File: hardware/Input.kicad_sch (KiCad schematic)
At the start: 15 parts, among them J10 Conn_Coaxial, J11 Conn_Coaxial, J12 Conn_Coaxial, J13 Conn_Coaxial, U22 SN74LVC2T45DCTR, U23 SN74LVC2T45DCTR

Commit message: update footprints to meet min pad clearance of 0.2mm
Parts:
- U22, U23: footprint Package_SO:VSSOP-8_2.3x2mm_P0.5mm -> kicad-lib:VSSOP-8_2.3x2mm_P0.5mm_TexasInstruments
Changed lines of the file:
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@@
 			)
 		)
-		(property "Footprint" "Package_SO:VSSOP-8_2.3x2mm_P0.5mm"
+		(property "Footprint" "kicad-lib:VSSOP-8_2.3x2mm_P0.5mm_TexasInstruments"
 			(at 152.4 93.98 0)
 			(effects
@@
 			)
 		)
-		(property "Footprint" "Package_SO:VSSOP-8_2.3x2mm_P0.5mm"
+		(property "Footprint" "kicad-lib:VSSOP-8_2.3x2mm_P0.5mm_TexasInstruments"
 			(at 152.4 152.4 0)
 			(effects

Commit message: update incorrect part numbers to match correct footprints
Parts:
- U22, U23: Link https://www.digikey.com/en/products/detail/texas-instruments/SN74LVC2T45DCTR/639457 -> https://www.digikey.com/en/products/detail/texas-instruments/SN74LVC2T45DCUR/657833; Manufacturer Number SN74LVC2T45DCTR -> SN74LVC2T45DCUR

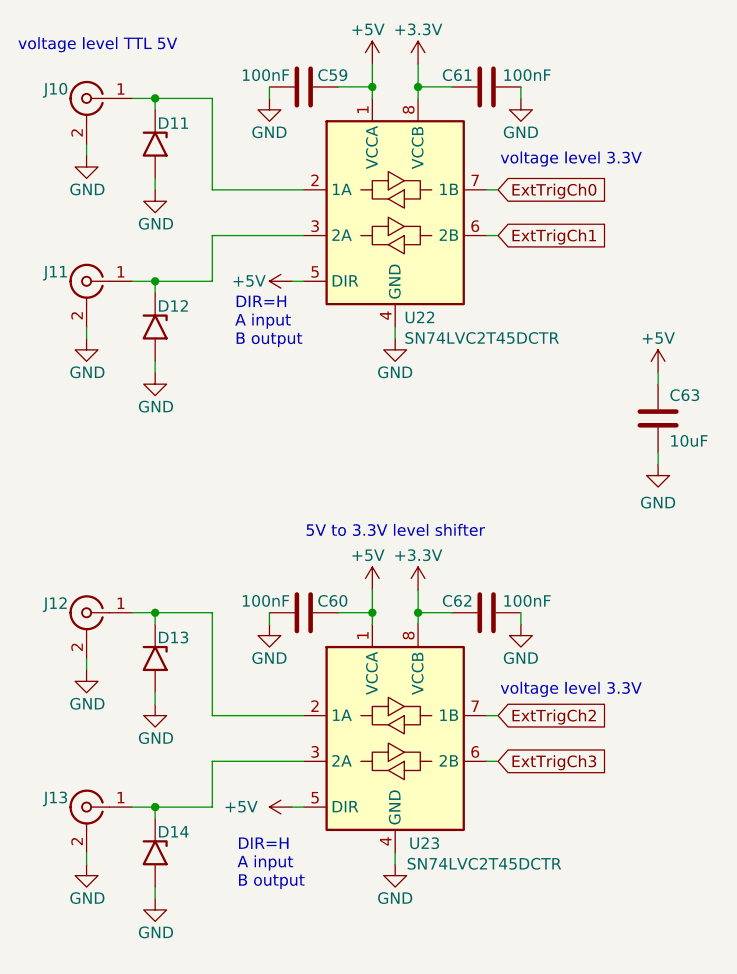
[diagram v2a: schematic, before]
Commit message: feat pcba updates (#69)
* replace INA181 w INA630

* flip c12; put ext triggers on gpio multiple of 8

* add pulldowns to external triggers

* change R3, R15, R16, R20, R21 package to 0402

* update 1K, 31K6, 10K resistors to 0.1%

* swap BNC connectors to taller versions

* move short-circuit pins to fall within multiple of 8 boundary

* add 1.0/1.1 hw pinout to config with default as 1.0

* update hardware author
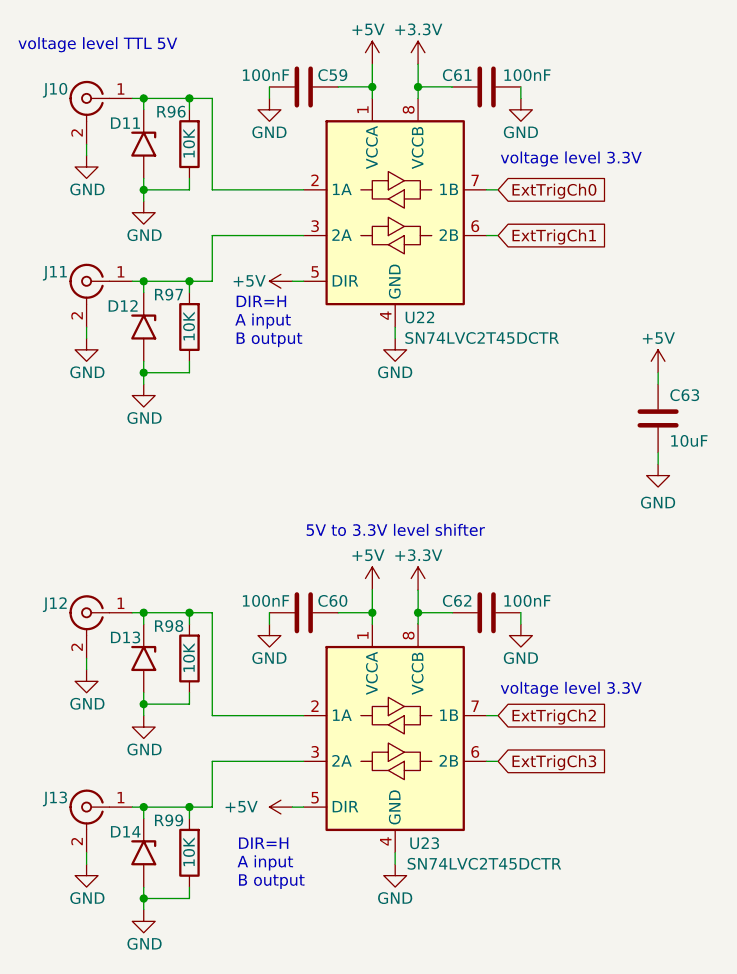
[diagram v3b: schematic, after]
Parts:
- added R96, R97, R98, R99: 10K, Resistor_SMD:R_0402_1005Metric, symbol Device:R
- J10, J11, J12, J13: footprint kicad-lib:BNC_TEConnectivity_CONBNC001_Vertical -> kicad-lib:BNC_AmphenolRF_031-5329-52RFX_Vertical; Link https://www.digikey.com/en/products/detail/te-connectivity-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 -> https://www.digikey.com/en/products/detail/amphenol-rf/031-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; Manufacturer TE Connectivity Linx -> Amphenol RF
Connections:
- net GND: now also R96.1, R97.1, R98.1, R99.1
- net at D14.1 (A1), J13.1 (In), U23.3 (2A): now also R99.2
- net at D11.1 (A1), J10.1 (In), U22.2 (1A): now also R96.2
- net at D12.1 (A1), J11.1 (In), U22.3 (2A): now also R97.2
- net at D13.1 (A1), J12.1 (In), U23.2 (1A): now also R98.2
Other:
- moved on the sheet: D11, D12, D13, D14
